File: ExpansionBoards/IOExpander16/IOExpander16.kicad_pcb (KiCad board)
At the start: 2 copper layers, 68.5 x 45 mm, 20 parts, among them J1 Screw_Terminal_01x02, J10 Screw_Terminal_01x02, J11 Screw_Terminal_01x02, J12 Screw_Terminal_01x02, J13 Screw_Terminal_01x02, J14 Screw_Terminal_01x02, J15 Screw_Terminal_01x02, J16 Screw_Terminal_01x02, J2 Screw_Terminal_01x05, J3 Conn_02x05_Counter_Clockwise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

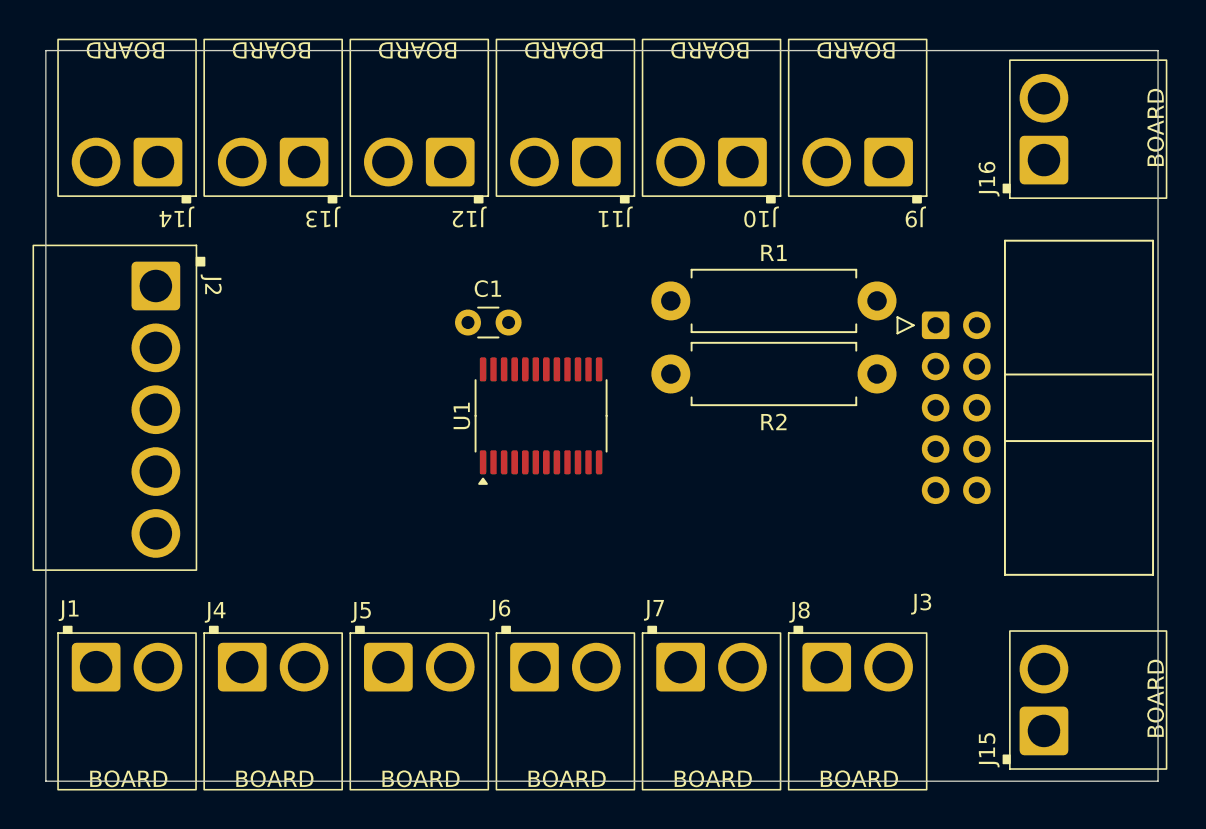
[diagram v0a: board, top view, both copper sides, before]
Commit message: IO expansion board layout compeleted ready for review.
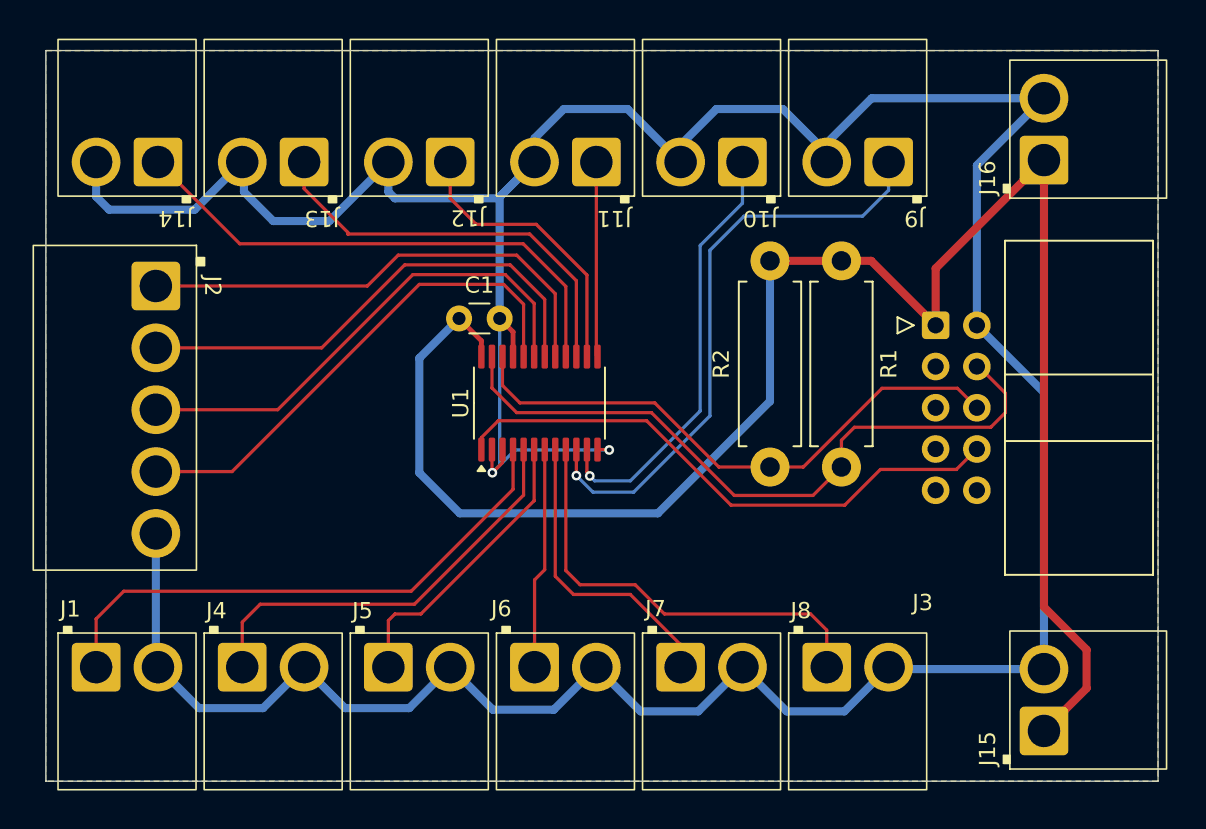
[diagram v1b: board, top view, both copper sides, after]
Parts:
- moved R1 10.8 mm to (130.5, 63.0), turned to -90 degrees
- moved R2 9.27 mm to (126.1, 63.0), turned to -90 degrees
- moved U1 0.79 mm to (111.9, 71.7)
- moved C1 0.60 mm to (107.0, 66.5)
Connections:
- J3 pad 3: /SPI_MOSI -> /SPI_CLK
- J3 pad 7: /SPI_CLK -> /SPI_MOSI
- U1 pad 22: /SDA -> /SCL
- U1 pad 23: /SCL -> /SDA
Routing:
- net GND: track 0.00 -> 225.4 mm, vias 0 -> 2
- net VDD: track 0.00 -> 109.7 mm
- net /SDA: track 0.00 -> 43.0 mm
- net /IO0_6: track 0.00 -> 36.7 mm, vias 0 -> 1
- net /SCL: track 0.00 -> 35.6 mm
- net /GPIO2: track 0.00 -> 35.3 mm
- net /IO0_0: track 0.00 -> 34.4 mm
- net /IO1_3: track 0.00 -> 32.6 mm
- net /IO1_7: track 0.00 -> 31.2 mm
- net /IO1_6: track 0.00 -> 30.8 mm
- net /IO1_5: track 0.00 -> 30.5 mm
- net /IO1_4: track 0.00 -> 30.2 mm
- net /IO0_5: track 0.00 -> 27.3 mm
- net /IO0_7: track 0.00 -> 26.8 mm, vias 0 -> 1
- net /IO0_1: track 0.00 -> 26.1 mm
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- added copper zone on B.Cu, net GND
- added copper zone on F.Cu, net GND
